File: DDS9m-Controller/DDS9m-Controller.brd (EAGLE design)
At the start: 100 x 33 mm, 15 parts, among them IC1 LTC6994-X, IC3 74LVC1G07DCK, X1 BNC-V

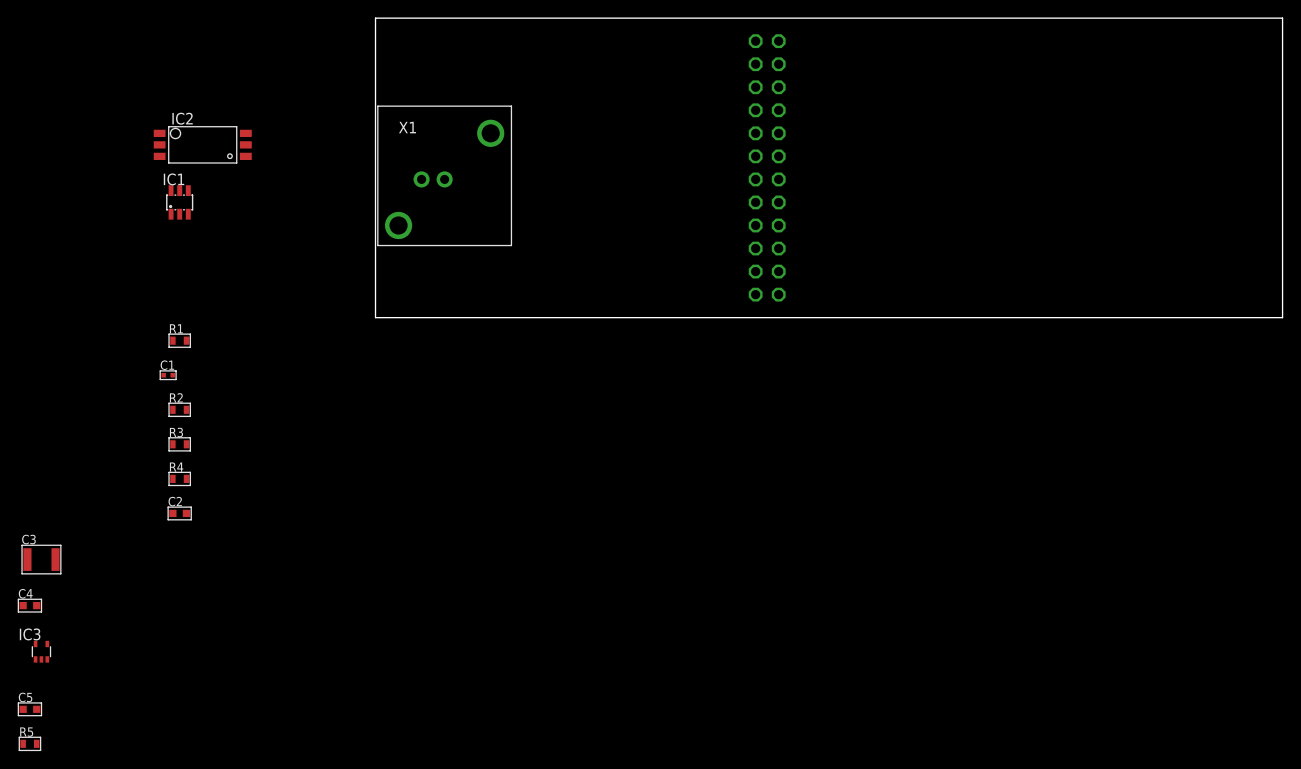
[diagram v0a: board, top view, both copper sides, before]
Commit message: Finished test layout
First pass at the schematic and board is ready to prototype.

DSB
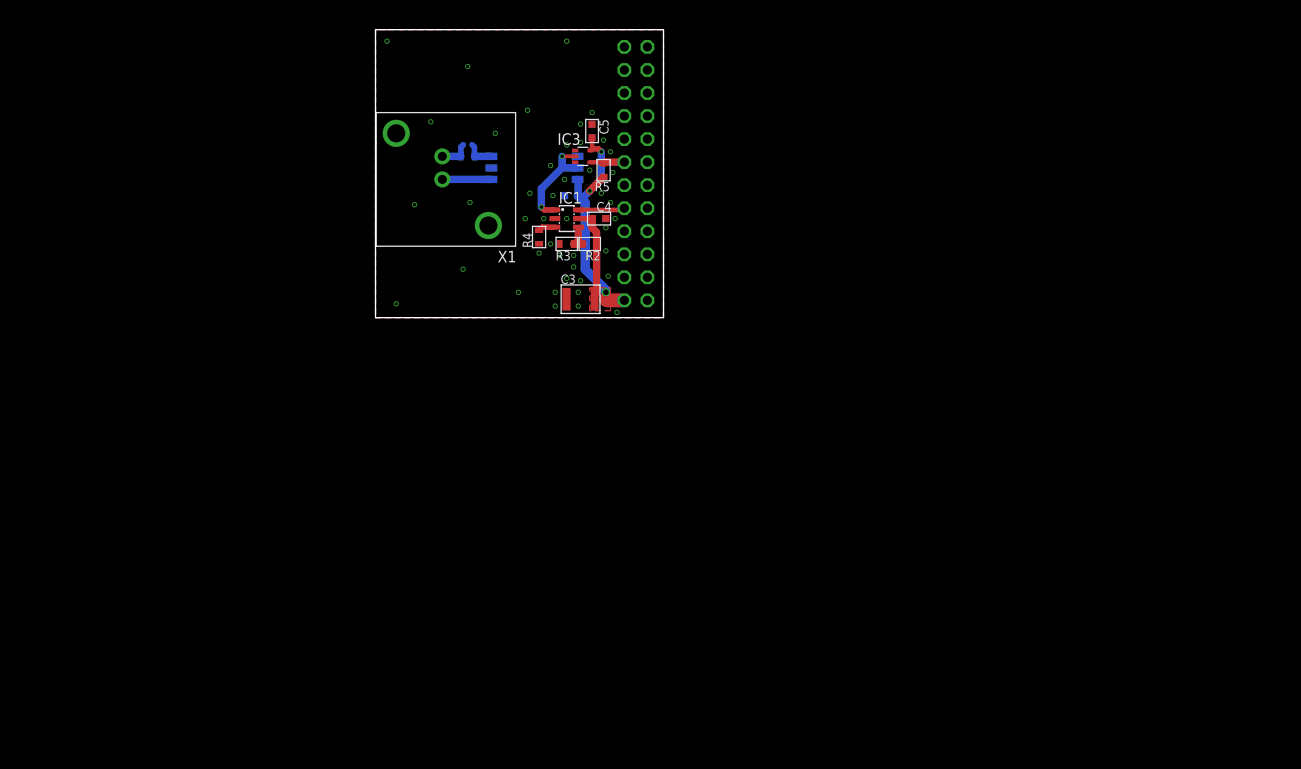
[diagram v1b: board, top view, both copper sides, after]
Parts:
- R4: value 50k -> 56k
- moved R5 89.4 mm to (25.1, 16.3), turned to 90 degrees
- moved C5 88.9 mm to (23.9, 20.6), turned to 270 degrees
- moved IC3 80.9 mm to (22.9, 17.8), turned to 270 degrees
- moved C4 75.9 mm to (24.6, 10.9)
- moved C3 66.0 mm to (22.6, 2.03), turned to 180 degrees
- moved C2 55.6 mm to (21.6, 13.5), flipped to the bottom
- moved R2 48.8 mm to (23.6, 8.13), turned to 180 degrees
- moved R3 48.1 mm to (21.1, 8.13)
- moved R4 47.8 mm to (18.0, 8.89), turned to 90 degrees
- moved IC1 42.7 mm to (21.1, 10.9), turned to 270 degrees
- moved C1 41.7 mm to (10.2, 19.1), flipped to the bottom
- moved R1 37.7 mm to (10.2, 17.8), flipped to the bottom, turned to 180 degrees
- moved IC2 36.7 mm to (17.5, 16.5), flipped to the bottom, turned to 180 degrees
- moved JP1 14.5 mm to (28.7, 15.9)
- moved X1 0.25 mm to (7.37, 15.2), turned to 270 degrees
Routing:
- net +3V3: track 0.00 -> 36.5 mm, vias 0 -> 3
- net INPUT: track 0.00 -> 11.3 mm, vias 0 -> 2
- net N$3: track 0.00 -> 5.41 mm
- net IRQ-: track 0.00 -> 5.13 mm
- net IOUD: track 0.00 -> 3.83 mm
- net N$2: track 0.00 -> 3.42 mm
- net N$1: track 0.00 -> 3.24 mm
- net N$4: track 0.00 -> 2.90 mm
- net N$6: track 0.00 -> 1.89 mm
- added copper zone on layer 1, net +3V3
- added copper zone on layer 1, net GND
- added copper zone on layer 16, net GND
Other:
- board size 100 x 33 mm -> 31.8 x 31.8 mm
